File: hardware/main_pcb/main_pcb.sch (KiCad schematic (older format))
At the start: 64 parts, among them J1 Boot, J2 Debug, J3 USB4110, J4 MEM2085, J5 CUI_SJ_3523, Q1 AM2336N, SW1 CS1102, SW2 CS1102, SW3 CS1102, SW4 CS1102, SW5 CK-JS102011SAQN, SW6 COM09426, U1 BQ21040, U2 STM32H533CET, U3 MCP1824, U4 IS67WVS4M8BLL-104NLA1, U5 MCP6009, U6 WF0200BTYAJDNN0, X1 ASE-16.000MHZ, Y1 CM315D32768HZFT

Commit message: Schematic cleanup, replace parts with latest selections, custom footprints for new parts.
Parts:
- removed J4: MEM2085, main_pcb:MEM2085, symbol local:MicroSD
- removed SW6: COM09426, main_pcb:COM09426, symbol local:COM09426
- removed U6: WF0200BTYAJDNN0, Connector_FFC-FPC:TE_4-1734839-0_1x40-1MP_P0.5mm_Horizontal, symbol local:WF0200BTYAJDNN0
- added C19, C20: 10u, Capacitor_SMD:C_0805_2012Metric, symbol Device:C_Small
- added J4: SD-4-B, main_pcb:SD-4-B, symbol local:SDCard
- added J6: SFV20R-2ST, main_pcb:FPC_1x20_P0.5mm_top, symbol local:Display
- added SW6: THB001P, main_pcb:THB001P, symbol local:THB001P
- added TP1, TP2, TP3, TP4: TestPoint_Small, TestPoint:TestPoint_Pad_D1.5mm, symbol Connector:TestPoint_Small
- D1: value LED -> 151031SS06000
- D3: value LED_Dual_AAC -> LTL-1BEHJ; symbol Device:LED_Dual_AAC -> Device:LED_Dual_ACA
- J5: value CUI_SJ_3523 -> STX-3500-3NTR
- Q1: value AM2336N -> SSM3K376R
- SW1, SW2, SW3, SW4: value CS1102 -> LL3301BF065QJ; footprint main_pcb:CS1102 -> main_pcb:LL3301-J; symbol local:CS1102 -> local:LL3301
- U2: value STM32H533CET -> STM32H523CET
- U3: value MCP1824 -> MCP1824T-3302E/OT
- U5: value MCP6009 -> MCP6009T-E/ST
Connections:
- wire segments 393 -> 435
- no-connect marks 27 -> 15
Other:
- note added: "3.3v Power"
- note added: "Analog Audio Out"
- note added: "Analog Power Filtering"
- note added: "Backlight Power\nConstant Current"
- note added: "Battery and Charger"
- note added: "Display\nConnector"
- note added: "Joystick and\nButtons"
- note added: "Program/Debug Interface"
- note added: "SD Card"
- note added: "Serial RAM"
- moved on the sheet: BT1, C1, C10, C11, C12, C13, C14, C15, C16, C17, C18, C2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

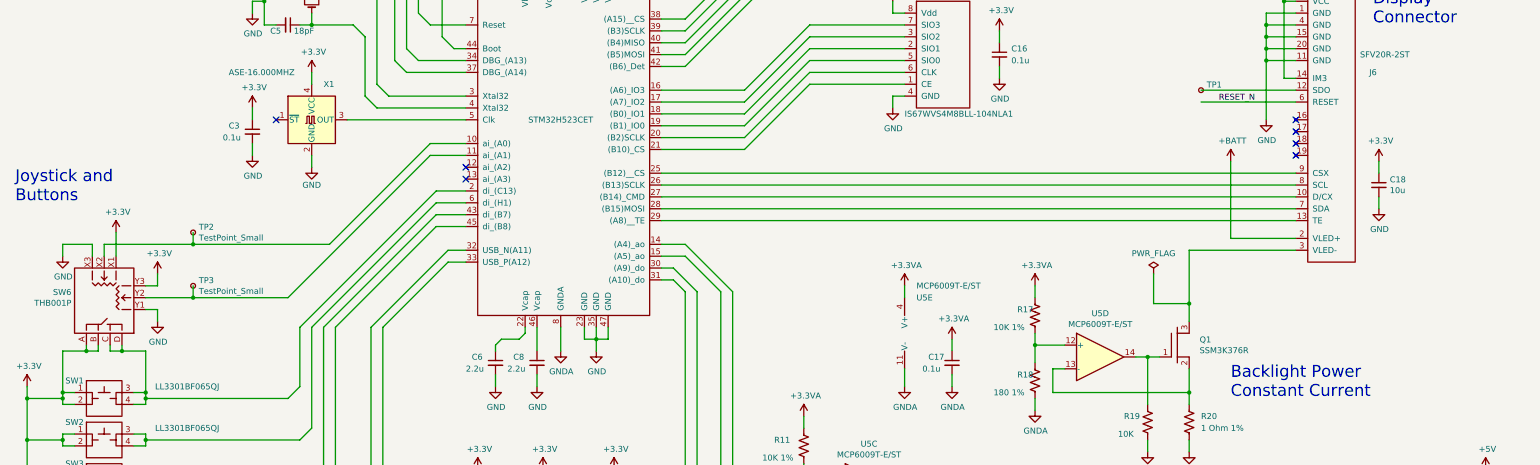
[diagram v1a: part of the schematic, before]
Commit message: Joystick orientation, some trace cleanup, add text to PCB silkscreen.
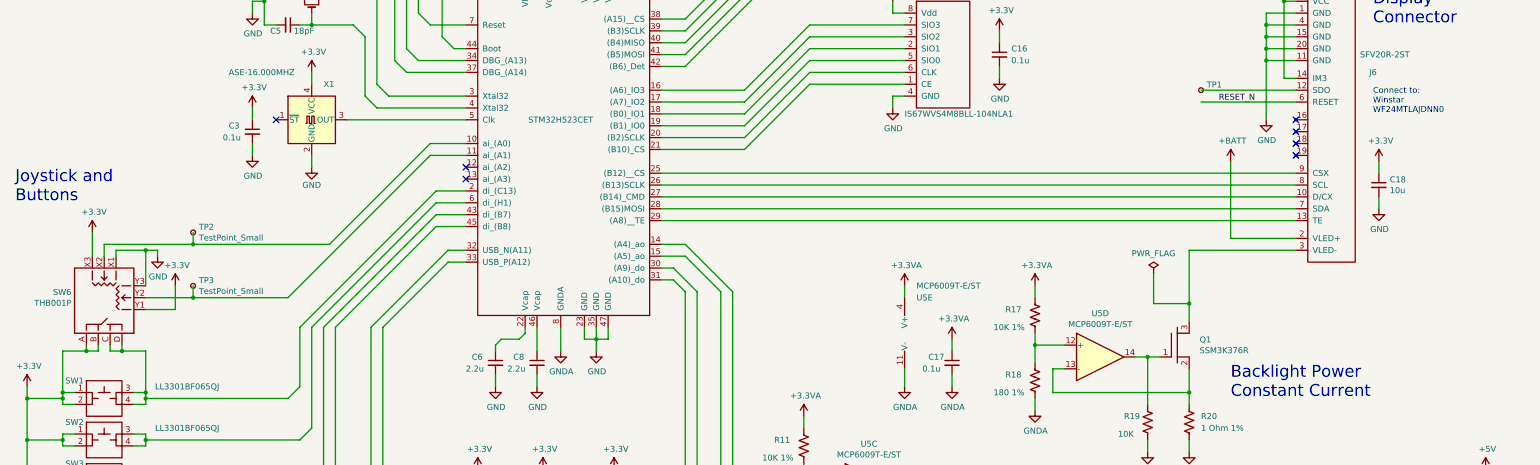
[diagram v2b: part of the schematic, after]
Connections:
- net +3V3: now also SW6.X3, SW6.Y1; no longer SW6.X1, SW6.Y3
- net GND: now also SW6.X1, SW6.Y3; no longer SW6.X3, SW6.Y1
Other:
- note added: "Connect to:\nWinstar\nWF24MTLAJDNN0"
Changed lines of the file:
@@
 U 1 1 66BB0A1F
 P 9300 5700
-F 0 "R17" H 9150 5750 50  0000 L CNN
+F 0 "R17" H 9050 5750 50  0000 L CNN
 F 1 "10K 1%" H 8950 5600 50  0000 L CNN
 F 2 "Resistor_SMD:R_0603_1608Metric" V 9340 5690 50  0001 C CNN
@@
 U 1 1 66BB5BCE
 P 9300 6250
-F 0 "R18" H 9150 6300 50  0000 L CNN
+F 0 "R18" H 9050 6300 50  0000 L CNN
 F 1 "180 1%" H 8950 6150 50  0000 L CNN
 F 2 "Resistor_SMD:R_0603_1608Metric" V 9340 6240 50  0001 C CNN
@@
 L power:+3.3V #PWR0106
 U 1 1 697A6C10
-P 1550 5000
-F 0 "#PWR0106" H 1550 4850 50  0001 C CNN
-F 1 "+3.3V" H 1565 5173 50  0000 C CNN
-F 2 "" H 1550 5000 50  0001 C CNN
-F 3 "" H 1550 5000 50  0001 C CNN
-	1    1550 5000
+P 1350 5000
+F 0 "#PWR0106" H 1350 4850 50  0001 C CNN
+F 1 "+3.3V" H 1365 5173 50  0000 C CNN
+F 2 "" H 1350 5000 50  0001 C CNN
+F 3 "" H 1350 5000 50  0001 C CNN
+	1    1350 5000
 	1    0    0    -1
 $EndComp
@@
 L power:+3.3V #PWR0107
 U 1 1 697A829D
-P 1900 5350
-F 0 "#PWR0107" H 1900 5200 50  0001 C CNN
-F 1 "+3.3V" H 1915 5523 50  0000 C CNN
-F 2 "" H 1900 5350 50  0001 C CNN
-F 3 "" H 1900 5350 50  0001 C CNN
-	1    1900 5350
-	1    0    0    -1
-$EndComp
-$Comp
-L power:GND #PWR0108
-U 1 1 697A952E
-P 1100 5200
-F 0 "#PWR0108" H 1100 4950 50  0001 C CNN
-F 1 "GND" H 1105 5027 50  0000 C CNN
-F 2 "" H 1100 5200 50  0001 C CNN
-F 3 "" H 1100 5200 50  0001 C CNN
-	1    1100 5200
+P 2050 5450
+F 0 "#PWR0107" H 2050 5300 50  0001 C CNN
+F 1 "+3.3V" H 2065 5623 50  0000 C CNN
+F 2 "" H 2050 5450 50  0001 C CNN
+F 3 "" H 2050 5450 50  0001 C CNN
+	1    2050 5450
 	1    0    0    -1
 $EndComp
@@
 L power:GND #PWR0109
 U 1 1 697AB44F
-P 1900 5750
-F 0 "#PWR0109" H 1900 5500 50  0001 C CNN
-F 1 "GND" H 1905 5577 50  0000 C CNN
-F 2 "" H 1900 5750 50  0001 C CNN
-F 3 "" H 1900 5750 50  0001 C CNN
-	1    1900 5750
-	1    0    0    -1
-$EndComp
-Wire Wire Line
-	1900 5350 1900 5450
-Wire Wire Line
-	1900 5450 1800 5450
-Wire Wire Line
-	1800 5650 1900 5650
-Wire Wire Line
-	1900 5650 1900 5750
-Wire Wire Line
-	1550 5200 1550 5000
-Wire Wire Line
-	1350 5200 1350 5100
-Wire Wire Line
-	1350 5100 1100 5100
-Wire Wire Line
-	1100 5100 1100 5200
+P 1900 5200
+F 0 "#PWR0109" H 1900 4950 50  0001 C CNN
+F 1 "GND" H 1905 5027 50  0000 C CNN
+F 2 "" H 1900 5200 50  0001 C CNN
+F 3 "" H 1900 5200 50  0001 C CNN
+	1    1900 5200
+	1    0    0    -1
+$EndComp
 Wire Wire Line
 	1100 6350 1100 6000
@@
 	3000 8400 2800 8400
 Connection ~ 2800 8400
+Wire Wire Line
+	1350 5000 1350 5200
+Wire Wire Line
+	1550 5200 1550 5150
+Wire Wire Line
+	1550 5150 1800 5150
+Wire Wire Line
+	1900 5150 1900 5200
+Wire Wire Line
+	1800 5450 1800 5150
+Connection ~ 1800 5150
+Wire Wire Line
+	1800 5150 1900 5150
+Wire Wire Line
+	2050 5450 2050 5650
+Wire Wire Line
+	2050 5650 1800 5650
+Text Notes 12150 4000 0    50   ~ 0
+Connect to:\nWinstar\nWF24MTLAJDNN0
 $EndSCHEMATC
